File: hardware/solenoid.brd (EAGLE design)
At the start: 37.3 x 34 mm, 35 parts, among them U2 AP2204R

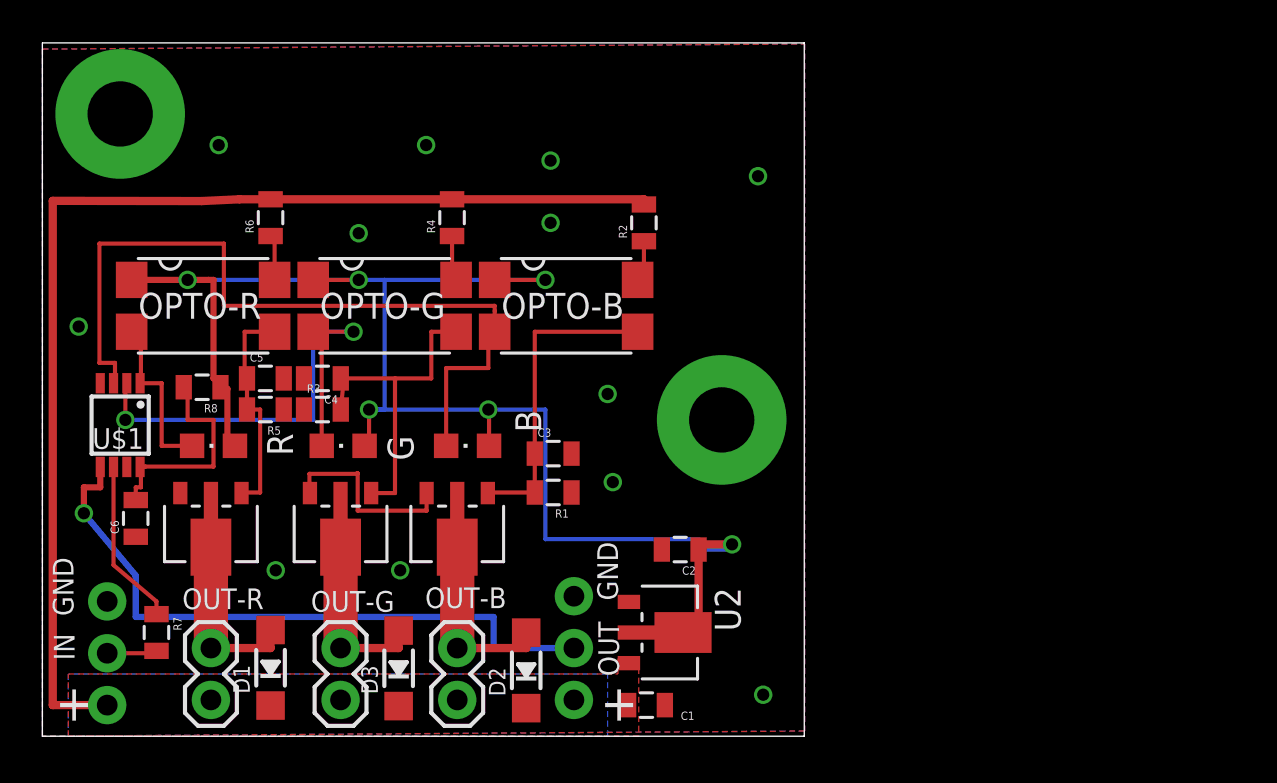
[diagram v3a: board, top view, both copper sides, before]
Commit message: Changed to TSDs instead of flyback diodes and increased the solder holw sizes
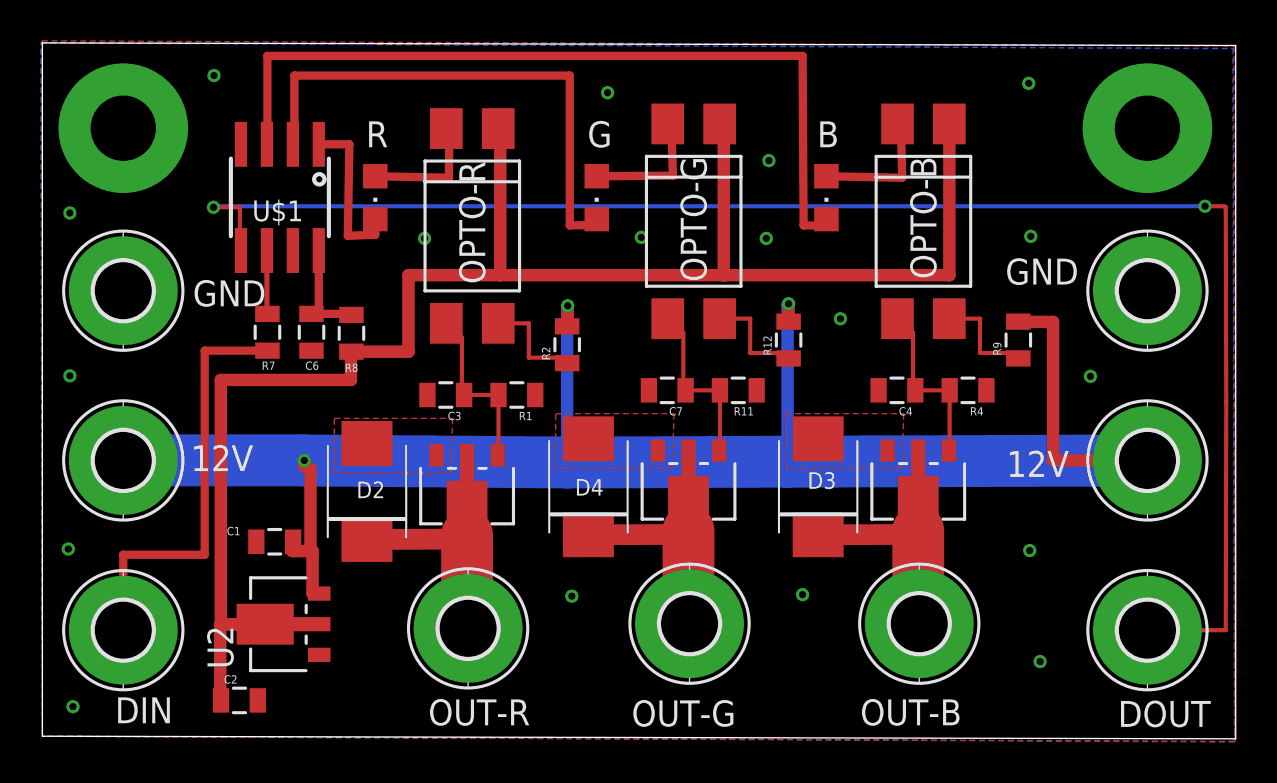
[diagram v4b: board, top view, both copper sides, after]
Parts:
- removed $T3: BSS606N, mishafarms:SOT89R
- removed C5: 400nf, SparkFun-Capacitors:0805
- removed D1: (no value), microbuilder:SOD-123
- removed R3, R5: 1000, SparkFun-Passives:0805
- removed R6: 220, SparkFun-Passives:0805
- added $T4: BSS606N, mishafarms:SOT89R
- added C7: 400nf, SparkFun-Capacitors:0805
- added D4: 36V, mishafarms:SMBJ
- added FRAME1: FRAME-LETTERNO_PACKAGE, SparkFun-Aesthetics:DUMMY
- added H1, H3, H4, H6: MOUNT-PAD-ROUND2.8, holes:2,8-PAD
- added R11: 1000, SparkFun-Passives:0805
- added R12, R9: 220, SparkFun-Passives:0805
- added U$2: IFL-LOGO, mishafarms:IFL-LOGO
- D2, D3: value (none) -> 36V; device microbuilder:SOD-123 -> mishafarms:SMBJ
- IN, OUT: value (none) -> MOUNT-PAD-ROUND2.8; device SparkFun-Connectors:1X03_NO_SILK -> holes:2,8-PAD
- OPTO-B, OPTO-G, OPTO-R: device optocoupler:SMD4 -> optocoupler:DIL4-SMD
- OUT-B, OUT-G, OUT-R: value (none) -> MOUNT-PAD-ROUND2.8; device SparkFun-Connectors:1X02 -> holes:2,8-PAD
- R4: value 220 -> 1000
- U$1: value WS2811S -> WS2811SSOP8; device mishafarms:MSOP8 -> mishafarms:SOIC8_150MIL
- U2: device mishafarms:SOT89R -> mishafarms:SOT89R@1
- moved $T2 28.4 mm to (42.9, 12.2)
- moved C4 28.1 mm to (41.9, 16.9)
- moved OUT 28.1 mm to (54.1, 5.19), turned to 0 degrees
- moved R4 26.7 mm to (45.3, 16.9), turned to 180 degrees
- moved S2 25.3 mm to (54.1, 29.8)
- moved OUT-B 22.9 mm to (43.0, 5.51), turned to 0 degrees
- moved C2 22.8 mm to (9.65, 1.75), turned to 0 degrees
- moved D3 22.4 mm to (38.0, 12.2)
- moved B 21.4 mm to (38.4, 26.4), turned to 180 degrees
- moved C1 19.9 mm to (11.4, 9.53), turned to 180 degrees
- moved U2 18.7 mm to (11.8, 5.49), turned to 90 degrees
- moved OPTO-B 18.0 mm to (43.2, 25.2), turned to 180 degrees
- moved OUT-G 17.5 mm to (31.7, 5.51), turned to 0 degrees
- moved G 17.4 mm to (27.2, 26.4), turned to 180 degrees
- moved OPTO-G 15.7 mm to (31.9, 25.2), turned to 180 degrees
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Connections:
- removed net N$10: $T3.2, C5.1, OPTO-R.3, R5.2
- removed net N$11: OPTO-R.4, R6.1
- removed net N$14: OUT.2, U$1.5
- removed net N$2: $T1.2, C3.1, OPTO-B.3, R1.2
- removed net N$3: OPTO-B.4, R2.1
- removed net N$30: IN.2, R7.2
- removed net N$4: $T1.3, $T1.4, D2.A, OUT-B.2
- new net IN: IN.B2,8, R7.2
- new net N$15: OPTO-B.4, R9.1
- new net N$16: B.A, OPTO-B.2
- new net N$19: $T4.1, C7.1, OPTO-G.3, R11.2
- new net N$20: OPTO-G.4, R12.1
- new net N$21: G.A, OPTO-G.2
- new net OUT: OUT.B2,8, U$1.5
- new net OUT-B: $T2.2, $T2.4, D3.C, OUT-B.B2,8
- new net OUT-G: $T4.2, $T4.4, D4.C, OUT-G.B2,8
- new net OUT-R: $T1.2, $T1.4, D2.C, OUT-R.B2,8
- net GND: now also $T1.3, $T2.3, $T4.3, C7.2, D2.A, D3.A, D4.A, H3.B2,8, H6.B2,8, R11.1, R4.1; no longer $T1.1, $T2.1, $T3.1, C5.2, IN.1, OUT.1, R3.1, R5.1
- net N$1: no longer OPTO-B.2
- net N$12: now also $T2.1, C4.1, OPTO-B.3, R4.2; no longer $T3.3, $T3.4, D1.A, OUT-R.2
- net N$5: no longer OPTO-G.2
- net N$6: now also $T1.1, C3.1, OPTO-R.3, R1.2; no longer $T2.2, C4.1, OPTO-G.3, R3.2
- net N$7: now also OPTO-R.4, R2.1; no longer OPTO-G.4, R4.1
- net N$8: now also OPTO-R.2, R.A; no longer $T2.3, $T2.4, D3.A, OUT-G.2
- net N$9: no longer OPTO-R.2
- net VCC: no longer B.A, G.A, R.A
- net VDD: now also H1.B2,8, H4.B2,8, R12.2, R9.2; no longer D1.C, D2.C, D3.C, IN.3, OUT-B.1, OUT-G.1, OUT-R.1, OUT.3, R4.2, R6.2
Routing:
- net OUT: track 0.00 -> 77.7 mm, vias 0 -> 2
- net VDD: track 56.6 -> 89.1 mm, vias 0 -> 3
- net N$14: track 32.1 -> 0.00 mm, vias 1 -> 0
- net IN: track 0.00 -> 20.8 mm
- net N$2: track 15.2 -> 0.00 mm
- net OUT-B: track 0.00 -> 13.2 mm
- net OUT-R: track 0.00 -> 13.2 mm
- net OUT-G: track 0.00 -> 13.2 mm
- net N$10: track 11.5 -> 0.00 mm
- net N$4: track 11.4 -> 0.00 mm
- net GND: track 9.42 -> 0.00 mm, vias 12 -> 18
- net N$19: track 0.00 -> 8.56 mm
- net N$6: track 16.4 -> 8.56 mm
- net N$16: track 0.00 -> 7.54 mm
- net N$21: track 0.00 -> 7.47 mm
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- removed copper zone on layer 1, net VDD
- removed copper zone on layer 16, net VDD
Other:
- board size 37.3 x 34 mm -> 58.5 x 34.1 mm
- board text added: "DIN"
- board text added: "DOUT"
- board text added: "WS2811 Solenoid driver 1A V1.0"
- board text removed: "IN"
- board text removed: "OUT"
- board text removed: "WS2811 Solenoid driver 1A V0.1"

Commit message: Fixed problem with reguslator having wrong footprint.
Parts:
- U2: device mishafarms:SOT89R@1 -> mishafarms:SOT89R
- moved FRAME1 34.4 mm to (-0.10, -1.04)
- moved C2 9.02 mm to (11.3, 10.6), turned to 180 degrees
- moved C1 8.26 mm to (10.5, 1.32), turned to 0 degrees
- renumbered H1 to 12V
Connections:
- net GND: now also U2.4
- net VCC: no longer U2.4
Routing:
- net VCC: track 85.5 -> 70.9 mm
- net VDD: track 89.1 -> 100.2 mm
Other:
- board text added: "WS2811 Solenoid driver 1A V1.1"
- board text removed: "WS2811 Solenoid driver 1A V1.0"
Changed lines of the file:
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@@
 <?xml version="1.0" encoding="utf-8"?>
 <!DOCTYPE eagle SYSTEM "eagle.dtd">
-<eagle version="8.2.0">
+<eagle version="8.2.1">
 <drawing>
 <settings>
@@
 <wire x1="58.4508" y1="33.833" x2="0" y2="33.96" width="0" layer="20"/>
 <wire x1="0" y1="33.96" x2="0" y2="0" width="0" layer="20"/>
-<text x="45.6184" y="10.7442" size="1.27" layer="22" font="vector" rot="MR0">WS2811 Solenoid driver 1A V1.0</text>
+<text x="45.6184" y="10.7442" size="1.27" layer="22" font="vector" rot="MR0">WS2811 Solenoid driver 1A V1.1</text>
 <wire x1="0" y1="173.38115" x2="173.38098125" y2="173.38115" width="0.025" layer="37"/>
 <polygon width="0" layer="51">
@@
 <attribute name="VALUE" x="14.8232" y="27.1866" size="1.016" layer="27" rot="R180"/>
 </element>
-<element name="U2" library="mishafarms" package="SOT89R@1" value="AP2204R" x="11.811" y="5.4864" smashed="yes" rot="R90">
+<element name="U2" library="mishafarms" package="SOT89R" value="AP2204R" x="11.811" y="5.4864" smashed="yes" rot="R90">
 <attribute name="NAME" x="9.356" y="3.2814" size="1.27" layer="25" rot="R90"/>
 <attribute name="VALUE" x="15.9916" y="0.4366" size="1.27" layer="27" rot="R90"/>
 <attribute name="VOLTAGE" value="5.0" x="11.811" y="5.4864" size="1.778" layer="27" rot="R90" display="off"/>
 </element>
-<element name="C1" library="SparkFun-Capacitors" package="0805" value="1uf" x="11.3792" y="9.525" smashed="yes" rot="R180">
-<attribute name="NAME" x="9.7028" y="10.2489" size="0.4064" layer="25" rot="R180"/>
-<attribute name="VALUE" x="9.9568" y="9.6266" size="0.4064" layer="27" rot="R180"/>
-</element>
-<element name="C2" library="SparkFun-Capacitors" package="0805" value="2.2uf" x="9.652" y="1.7526"/>
+<element name="C1" library="SparkFun-Capacitors" package="0805" value="1uf" x="10.4648" y="1.3208" smashed="yes">
+<attribute name="NAME" x="12.1412" y="0.5969" size="0.4064" layer="25"/>
+<attribute name="VALUE" x="11.8872" y="1.2192" size="0.4064" layer="27"/>
+</element>
+<element name="C2" library="SparkFun-Capacitors" package="0805" value="2.2uf" x="11.3284" y="10.6172" rot="R180"/>
 <element name="S1" library="SparkFun-Electromechanical" package="STANDOFF-ELECTRICAL" value="STANDOFF_ELECTRICAL" x="3.9624" y="29.781496875"/>
 <element name="S2" library="SparkFun-Electromechanical" package="STANDOFF-ELECTRICAL" value="STANDOFF_ELECTRICAL" x="54.1274" y="29.781496875"/>
@@
 <element name="OUT-B" library="holes" package="2,8-PAD" value="MOUNT-PAD-ROUND2.8" x="42.9514" y="5.5118"/>
 <element name="U$2" library="mishafarms" package="IFL-LOGO" value="IFL-LOGO" x="29.5402" y="22.987"/>
-<element name="H1" library="holes" package="2,8-PAD" value="MOUNT-PAD-ROUND2.8" x="54.1274" y="13.508565625" smashed="yes"/>
+<element name="12V" library="holes" package="2,8-PAD" value="MOUNT-PAD-ROUND2.8" x="54.1274" y="13.508565625" smashed="yes"/>
 <element name="IN" library="holes" package="2,8-PAD" value="MOUNT-PAD-ROUND2.8" x="3.9624" y="5.1943"/>
 <element name="H3" library="holes" package="2,8-PAD" value="MOUNT-PAD-ROUND2.8" x="3.9624" y="21.82283125" smashed="yes"/>
@@
 <element name="OUT" library="holes" package="2,8-PAD" value="MOUNT-PAD-ROUND2.8" x="54.1274" y="5.1943" smashed="yes"/>
 <element name="H6" library="holes" package="2,8-PAD" value="MOUNT-PAD-ROUND2.8" x="54.1274" y="21.82283125" smashed="yes"/>
-<element name="FRAME1" library="SparkFun-Aesthetics" package="DUMMY" value="FRAME-LETTERNO_PACKAGE" x="-27.7876" y="-21.4884">
-<attribute name="CREVISON" value="1.0" x="-27.7876" y="-21.4884" size="1.778" layer="27" display="off"/>
-<attribute name="DESIGNER" value="Michael L. Weiss" x="-27.7876" y="-21.4884" size="1.778" layer="27" display="off"/>
-<attribute name="VERSION" value="v1.0" x="-27.7876" y="-21.4884" size="1.778" layer="27" display="off"/>
+<element name="FRAME1" library="SparkFun-Aesthetics" package="DUMMY" value="FRAME-LETTERNO_PACKAGE" x="-0.1016" y="-1.0414">
+<attribute name="CREVISON" value="1.1" x="-0.1016" y="-1.0414" size="1.778" layer="27" display="off"/>
+<attribute name="DESIGNER" value="Michael L. Weiss" x="-0.1016" y="-1.0414" size="1.778" layer="27" display="off"/>
+<attribute name="VERSION" value="v1.0" x="-0.1016" y="-1.0414" size="1.778" layer="27" display="off"/>
 </element>
 </elements>
@@
 <via x="51.3334" y="17.6276" extent="1-16" drill="0.35"/>
 <via x="48.8696" y="3.6576" extent="1-16" drill="0.35"/>
+<contactref element="U2" pad="4"/>
 </signal>
 <signal name="VDD">
 <contactref element="U2" pad="1"/>
 <contactref element="C1" pad="1"/>
-<contactref element="H1" pad="B2,8"/>
+<contactref element="12V" pad="B2,8"/>
 <contactref element="H4" pad="B2,8"/>
-<wire x1="13.561" y1="6.9864" x2="13.2334" y2="6.9864" width="0.6096" layer="1"/>
-<wire x1="13.2334" y1="6.9864" x2="13.2334" y2="9.0678" width="0.6096" layer="1"/>
-<wire x1="13.1318" y1="9.0678" x2="12.2538" y2="9.0678" width="0.6096" layer="1"/>
-<wire x1="12.2538" y1="9.0678" x2="12.2792" y2="9.525" width="0.6096" layer="1"/>
-<wire x1="3.9624" y1="13.508565625" x2="12.8016" y2="13.508565625" width="2.54" layer="16"/>
-<wire x1="25.7048" y1="13.406965625" x2="12.827" y2="13.508565625" width="2.54" layer="16"/>
-<wire x1="36.501584375" y1="13.445559375" x2="25.7048" y2="13.406965625" width="2.54" layer="16"/>
+<wire x1="25.7048" y1="13.406965625" x2="36.501584375" y2="13.445559375" width="2.54" layer="16"/>
 <wire x1="36.501584375" y1="13.445559375" x2="54.1274" y2="13.508565625" width="2.54" layer="16"/>
-<wire x1="12.8016" y1="13.508565625" x2="12.827" y2="13.508565625" width="0.6096" layer="16"/>
-<wire x1="13.2334" y1="9.0678" x2="13.1318" y2="9.0678" width="0.6096" layer="1"/>
-<wire x1="13.1318" y1="9.0678" x2="13.1318" y2="13.1064" width="0.6096" layer="1"/>
-<wire x1="13.1318" y1="13.1064" x2="12.827" y2="13.2334" width="0.6096" layer="1"/>
-<wire x1="12.827" y1="13.2334" x2="12.827" y2="13.508565625" width="0.6096" layer="1"/>
-<via x="12.827" y="13.508565625" extent="1-16" drill="0.35"/>
 <contactref element="R2" pad="2"/>
 <contactref element="R12" pad="2"/>
@@
 <wire x1="36.5506" y1="21.1836" x2="36.501584375" y2="21.134584375" width="0.6096" layer="16"/>
 <wire x1="36.501584375" y1="21.134584375" x2="36.501584375" y2="13.445559375" width="0.6096" layer="16"/>
+<wire x1="3.9624" y1="13.508565625" x2="9.2964" y2="13.508565625" width="2.54" layer="16"/>
+<wire x1="9.2964" y1="13.508565625" x2="25.459515625" y2="13.508565625" width="2.54" layer="16"/>
+<wire x1="25.459515625" y1="13.508565625" x2="25.7048" y2="13.406965625" width="2.54" layer="16" curve="-45"/>
+<wire x1="9.2964" y1="13.508565625" x2="8.9662" y2="13.178365625" width="0.4064" layer="16" curve="90"/>
+<via x="8.9662" y="2.4384" extent="1-16" drill="0.35"/>
+<wire x1="8.9662" y1="2.4384" x2="8.9408" y2="2.413" width="0.4064" layer="1" curve="90"/>
+<wire x1="8.9408" y1="2.413" x2="8.9408" y2="1.4224" width="0.6096" layer="1"/>
+<wire x1="8.9408" y1="1.4224" x2="9.4632" y2="1.4224" width="0.6096" layer="1"/>
+<wire x1="9.4632" y1="1.4224" x2="9.5648" y2="1.3208" width="0.4064" layer="1" curve="-90"/>
+<wire x1="8.9662" y1="13.178365625" x2="8.9662" y2="2.4384" width="0.6096" layer="16"/>
+<wire x1="9.5648" y1="1.3208" x2="9.8044" y2="1.5604" width="0.6096" layer="1" curve="90"/>
+<wire x1="9.8044" y1="1.5604" x2="9.8044" y2="2.9464" width="0.6096" layer="1"/>
+<wire x1="9.8044" y1="2.9464" x2="13.589" y2="2.9464" width="0.6096" layer="1"/>
+<wire x1="13.589" y1="2.9464" x2="13.6398" y2="2.9972" width="0.4064" layer="1" curve="90"/>
+<wire x1="13.6398" y1="2.9972" x2="13.561" y2="3.076" width="0.4064" layer="1" curve="-90"/>
+<wire x1="13.561" y1="3.076" x2="13.561" y2="3.9864" width="0.6096" layer="1"/>
 </signal>
 <signal name="VCC">
 <contactref element="U2" pad="3"/>
 <contactref element="C2" pad="1"/>
-<contactref element="U2" pad="4"/>
 <contactref element="R8" pad="1"/>
 <contactref element="OPTO-R" pad="1"/>
@@
 <wire x1="33.1724" y1="29.9922" x2="33.3756" y2="29.9922" width="0.6096" layer="1"/>
 <wire x1="33.3756" y1="29.9922" x2="33.3756" y2="22.5806" width="0.6096" layer="1"/>
-<wire x1="8.752" y1="1.7526" x2="8.7122" y2="1.7924" width="0.6096" layer="1"/>
-<wire x1="8.7122" y1="5.461" x2="8.7122" y2="1.7924" width="0.6096" layer="1"/>
-<wire x1="8.7376" y1="5.4864" x2="8.7122" y2="5.461" width="0.6096" layer="1"/>
-<wire x1="15.1384" y1="18.8358" x2="15.113" y2="18.8104" width="0.6096" layer="1"/>
-<wire x1="15.113" y1="17.4498" x2="8.7376" y2="17.4498" width="0.6096" layer="1"/>
-<wire x1="8.7376" y1="17.4498" x2="8.7376" y2="5.4864" width="0.6096" layer="1"/>
-<wire x1="15.113" y1="18.8104" x2="15.113" y2="17.4498" width="0.6096" layer="1"/>
-<wire x1="13.211" y1="5.4864" x2="8.7376" y2="5.4864" width="0.6096" layer="1"/>
-<wire x1="8.7376" y1="5.4864" x2="8.7122" y2="5.4864" width="0.254" layer="1"/>
-<wire x1="8.7122" y1="5.4864" x2="8.7122" y2="5.461" width="0.254" layer="1"/>
-<wire x1="10.911" y1="5.4864" x2="8.7376" y2="5.4864" width="0.6096" layer="1"/>
+<wire x1="15.113" y1="18.8104" x2="15.1384" y2="18.8358" width="0.6096" layer="1"/>
+<wire x1="13.561" y1="6.9864" x2="12.827" y2="6.9864" width="0.6096" layer="1"/>
+<wire x1="12.827" y1="17.1704" x2="15.113" y2="17.1704" width="0.6096" layer="1"/>
+<wire x1="12.827" y1="6.9864" x2="12.827" y2="10.7188" width="0.6096" layer="1"/>
+<wire x1="12.827" y1="10.7188" x2="12.827" y2="17.1704" width="0.6096" layer="1"/>
+<wire x1="15.113" y1="17.1704" x2="15.113" y2="18.8104" width="0.6096" layer="1"/>
+<wire x1="12.827" y1="10.7188" x2="12.2284" y2="10.7188" width="0.6096" layer="1"/>
+<wire x1="12.2284" y1="10.7188" x2="12.2284" y2="10.6172" width="0.6096" layer="1"/>
 </signal>
 <signal name="N$5">

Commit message: Changed from 470nf to 1uf for the filter cap now I get no chatter on my solenoids when I have the level at 127.
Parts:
- C3, C4, C7: value 400nf -> 1uf
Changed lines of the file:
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@@
 <attribute name="VALUE" x="13.7668" y="27.6479" size="1.27" layer="27" rot="R270"/>
 </element>
-<element name="C3" library="SparkFun-Capacitors" package="0805" value="400nf" x="19.7612" y="16.7132" rot="R180"/>
+<element name="C3" library="SparkFun-Capacitors" package="0805" value="1uf" x="19.7612" y="16.7132" rot="R180"/>
 <element name="D2" library="mishafarms" package="SMBJ" value="36V" x="15.9004" y="11.9888" smashed="yes" rot="R90">
 <attribute name="NAME" x="16.7894" y="12.4714" size="0.8128" layer="25" rot="R180"/>
@@
 <attribute name="VALUE" x="24.6126" y="27.6479" size="1.27" layer="27" rot="R270"/>
 </element>
-<element name="C7" library="SparkFun-Capacitors" package="0805" value="400nf" x="30.607" y="16.9418" rot="R180"/>
+<element name="C7" library="SparkFun-Capacitors" package="0805" value="1uf" x="30.607" y="16.9418" rot="R180"/>
 <element name="D4" library="mishafarms" package="SMBJ" value="36V" x="26.7462" y="12.2174" smashed="yes" rot="R90">
 <attribute name="NAME" x="26.0858" y="11.7856" size="0.8128" layer="25"/>
@@
 <attribute name="VALUE" x="35.8648" y="27.6479" size="1.27" layer="27" rot="R270"/>
 </element>
-<element name="C4" library="SparkFun-Capacitors" package="0805" value="400nf" x="41.8592" y="16.9418" rot="R180"/>
+<element name="C4" library="SparkFun-Capacitors" package="0805" value="1uf" x="41.8592" y="16.9418" rot="R180"/>
 <element name="D3" library="mishafarms" package="SMBJ" value="36V" x="37.9984" y="12.2174" smashed="yes" rot="R90">
 <attribute name="NAME" x="38.8874" y="12.9286" size="0.8128" layer="25" rot="R180"/>
